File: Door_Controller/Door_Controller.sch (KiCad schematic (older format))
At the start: 0 parts

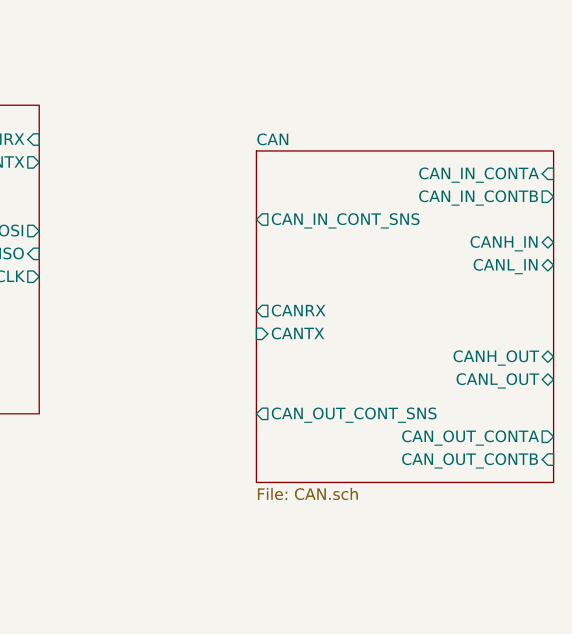
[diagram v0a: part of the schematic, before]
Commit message: rm CAN continuity
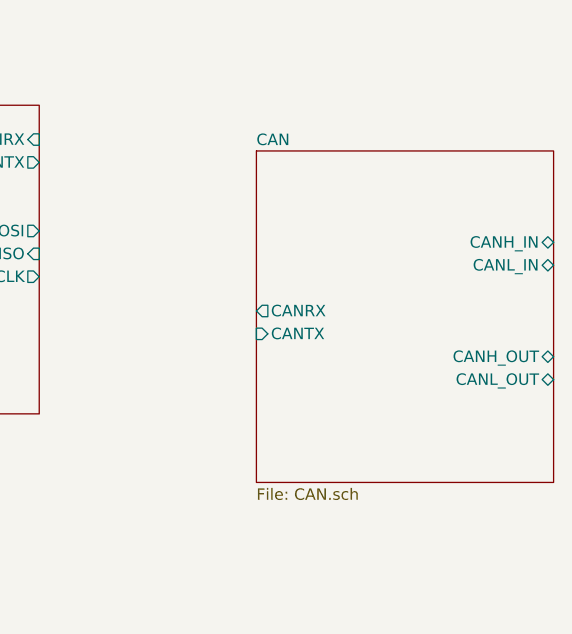
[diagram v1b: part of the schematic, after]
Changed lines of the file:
@@
 F0 "CAN" 50
 F1 "CAN.sch" 50
-F2 "CAN_IN_CONTA" I R 6000 2000 50
-F3 "CAN_IN_CONTB" O R 6000 2100 50
-F4 "CAN_OUT_CONTB" I R 6000 3250 50
-F5 "CAN_OUT_CONTA" O R 6000 3150 50
-F6 "CAN_IN_CONT_SNS" O L 4700 2200 50
-F7 "CAN_OUT_CONT_SNS" O L 4700 3050 50
 F8 "CANH_IN" B R 6000 2300 50
 F9 "CANL_IN" B R 6000 2400 50
